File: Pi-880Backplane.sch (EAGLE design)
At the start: 2 parts

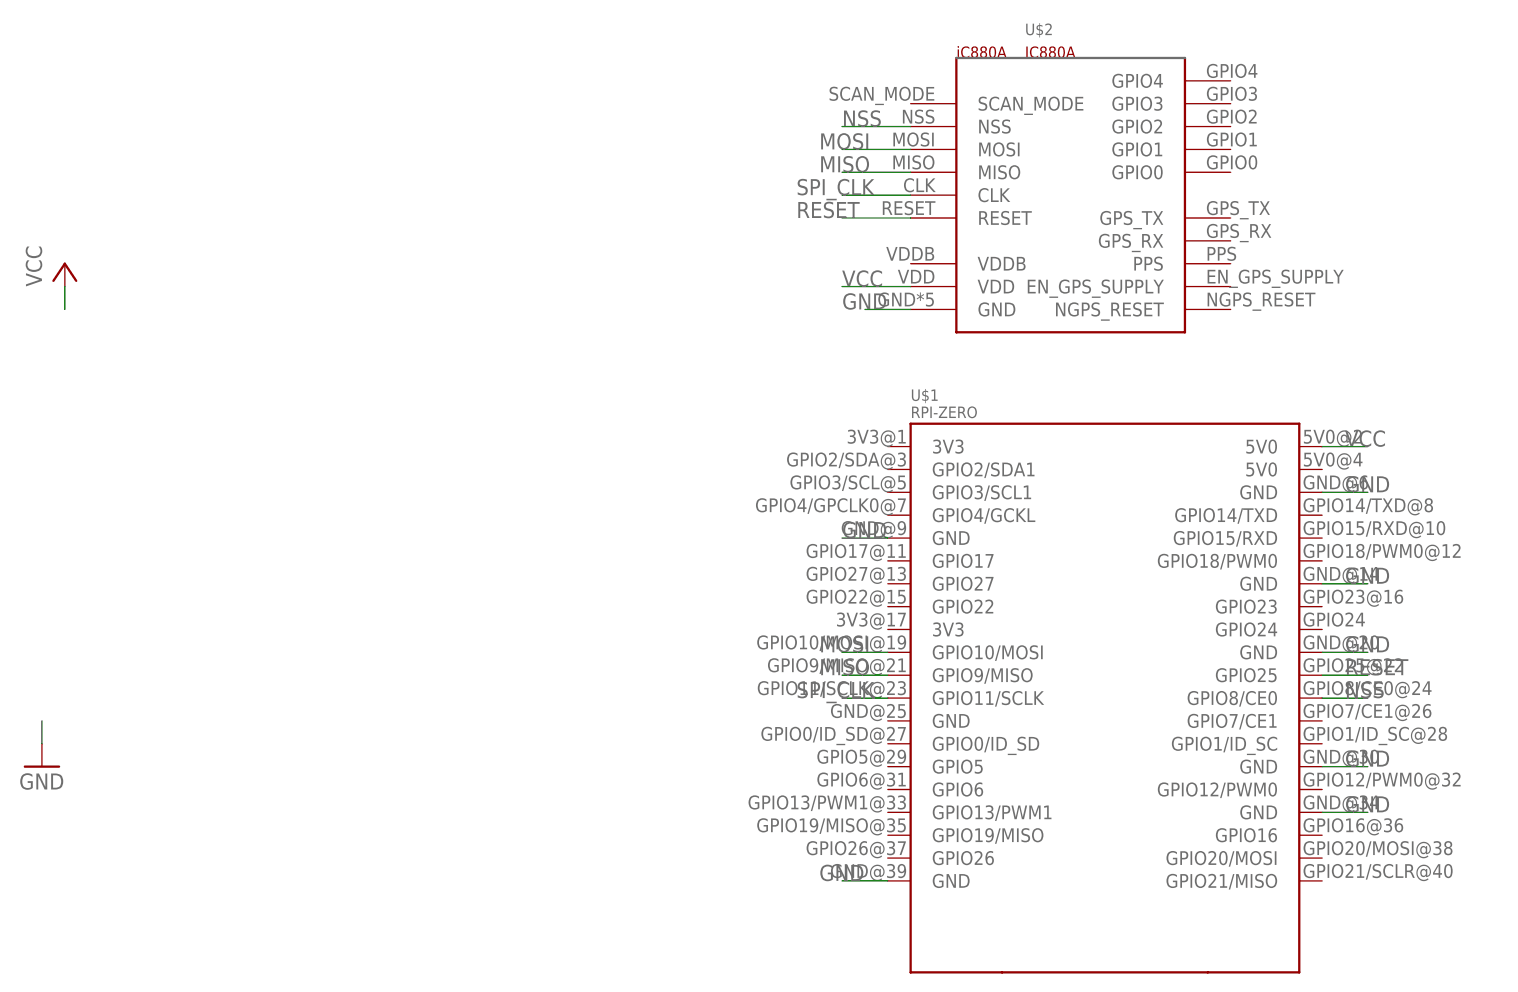
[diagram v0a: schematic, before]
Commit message: Drill holes bigger
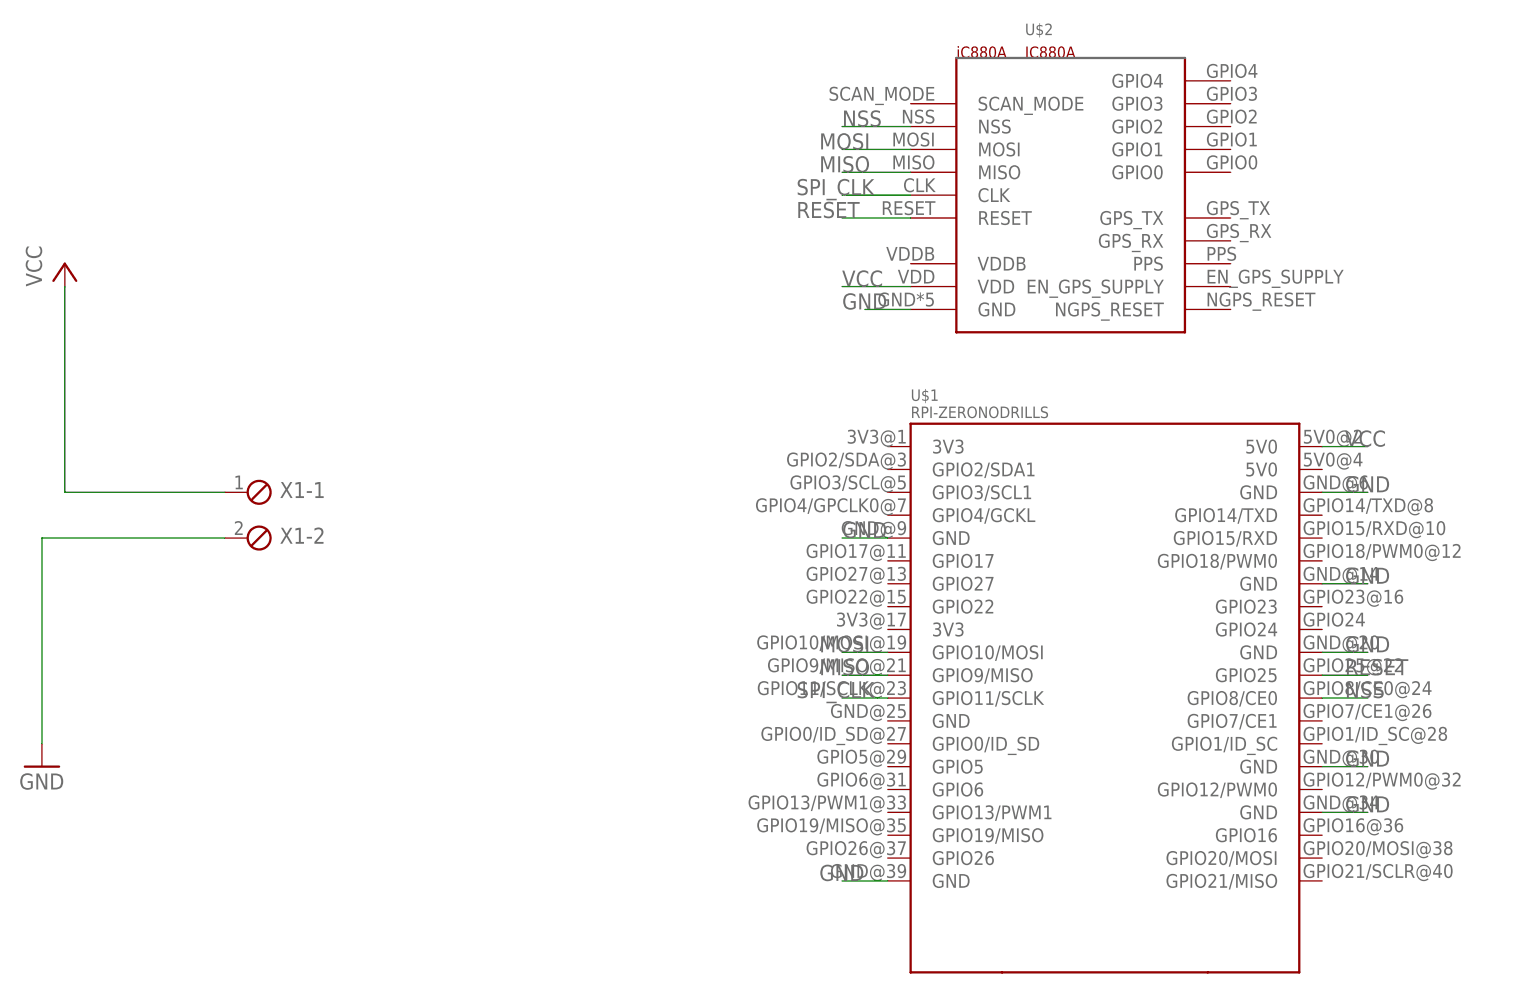
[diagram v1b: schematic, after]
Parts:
- added X1: (no value), con-phoenix-254:MPT2
- U$1: value RPI-ZERO -> RPI-ZERONODRILLS; device RPI-Zero:RPI-ZERO -> tobias:RPI-ZERONODRILLS
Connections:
- net GND: now also X1-2.1
- net VCC: now also X1-1.1
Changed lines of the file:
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@@
 <part name="P+2" library="supply1" deviceset="VCC" device=""/>
 <part name="GND1" library="supply1" deviceset="GND" device=""/>
-<part name="U$1" library="RPI-Zero" deviceset="RPI-ZERO" device=""/>
+<part name="U$1" library="tobias" deviceset="RPI-ZERO" device="NODRILLS"/>
 <part name="U$2" library="tobias" deviceset="IC880A" device=""/>
+<part name="X1" library="con-phoenix-254" deviceset="MPT2" device=""/>
 </parts>
 <sheets>
@@
 <instance part="U$1" gate="G$1" x="114.3" y="25.4"/>
 <instance part="U$2" gate="G$1" x="111.76" y="83.82"/>
+<instance part="X1" gate="-1" x="20.32" y="50.8"/>
+<instance part="X1" gate="-2" x="20.32" y="45.72"/>
 </instances>
 <busses>
@@
 <segment>
 <pinref part="P+2" gate="VCC" pin="VCC"/>
-<wire x1="0" y1="73.66" x2="0" y2="71.12" width="0.1524" layer="91"/>
+<pinref part="X1" gate="-1" pin="1"/>
+<wire x1="17.78" y1="50.8" x2="0" y2="50.8" width="0.1524" layer="91"/>
+<wire x1="0" y1="50.8" x2="0" y2="73.66" width="0.1524" layer="91"/>
 </segment>
 <segment>
@@
 <segment>
 <pinref part="GND1" gate="1" pin="GND"/>
-<wire x1="-2.54" y1="22.86" x2="-2.54" y2="25.4" width="0.1524" layer="91"/>
+<pinref part="X1" gate="-2" pin="1"/>
+<wire x1="17.78" y1="45.72" x2="-2.54" y2="45.72" width="0.1524" layer="91"/>
+<wire x1="-2.54" y1="45.72" x2="-2.54" y2="22.86" width="0.1524" layer="91"/>
 </segment>
 <segment>

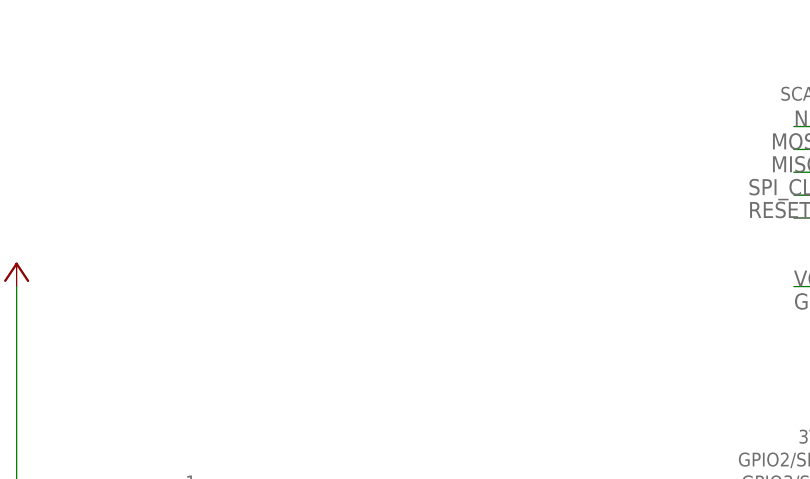
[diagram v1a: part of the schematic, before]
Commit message: Better SMA mount
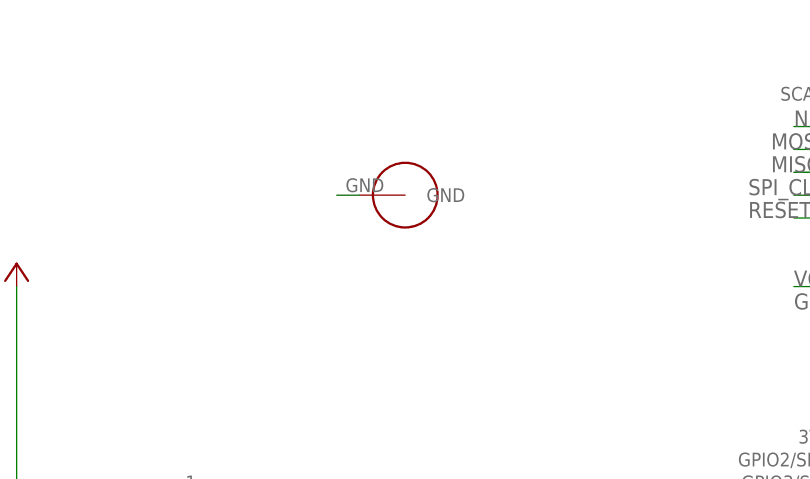
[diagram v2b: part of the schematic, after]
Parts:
- added U$3: SMA-PIGTAIL-MOUNT, tobias:SMA-PIGTAIL-MOUNT
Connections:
- net GND: now also U$3.GND
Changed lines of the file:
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@@
 <part name="U$2" library="tobias" deviceset="IC880A" device=""/>
 <part name="X1" library="con-phoenix-254" deviceset="MPT2" device=""/>
+<part name="U$3" library="tobias" deviceset="SMA-PIGTAIL-MOUNT" device=""/>
 </parts>
 <sheets>
@@
 <instance part="X1" gate="-1" x="20.32" y="50.8"/>
 <instance part="X1" gate="-2" x="20.32" y="45.72"/>
+<instance part="U$3" gate="G$1" x="43.18" y="83.82"/>
 </instances>
 <busses>
@@
 <label x="142.24" y="15.24" size="1.778" layer="95"/>
 </segment>
+<segment>
+<pinref part="U$3" gate="G$1" pin="GND"/>
+<wire x1="38.1" y1="83.82" x2="35.56" y2="83.82" width="0.1524" layer="91"/>
+</segment>
 </net>
